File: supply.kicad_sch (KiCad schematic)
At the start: 156 parts, among them J7 BarrelJack_3167288, J8 JST_SH_1x4_BM04B-SRSS-TB-LF-SN, Q12 SI7613DN-T1-GE3, Q13 SI7613DN-T1-GE3, Q14 BSS138PW, Q15 BSS138PW, Q16 BSS138PW, Q17 BSS138PW, SW4 SW_CVS-08TB, SW5 SW_KMR211NGLFS_SMD, U17 LTC4412IS6, U18 LTC4412IS6, U19 MPM54304GMN, U20 MPM54304GMN, U21 NCP718BSN330T1G, U22 MAX16150A_SOT, U25 PAC1954T-E_VQFN, U26 MAX812REUS+T, U27 MP8869S, U28 XC6230H001ER-G, U29 MCP4726A0T-E_MAY, U30 PAC1954T-E_VQFN, U31 LM3880

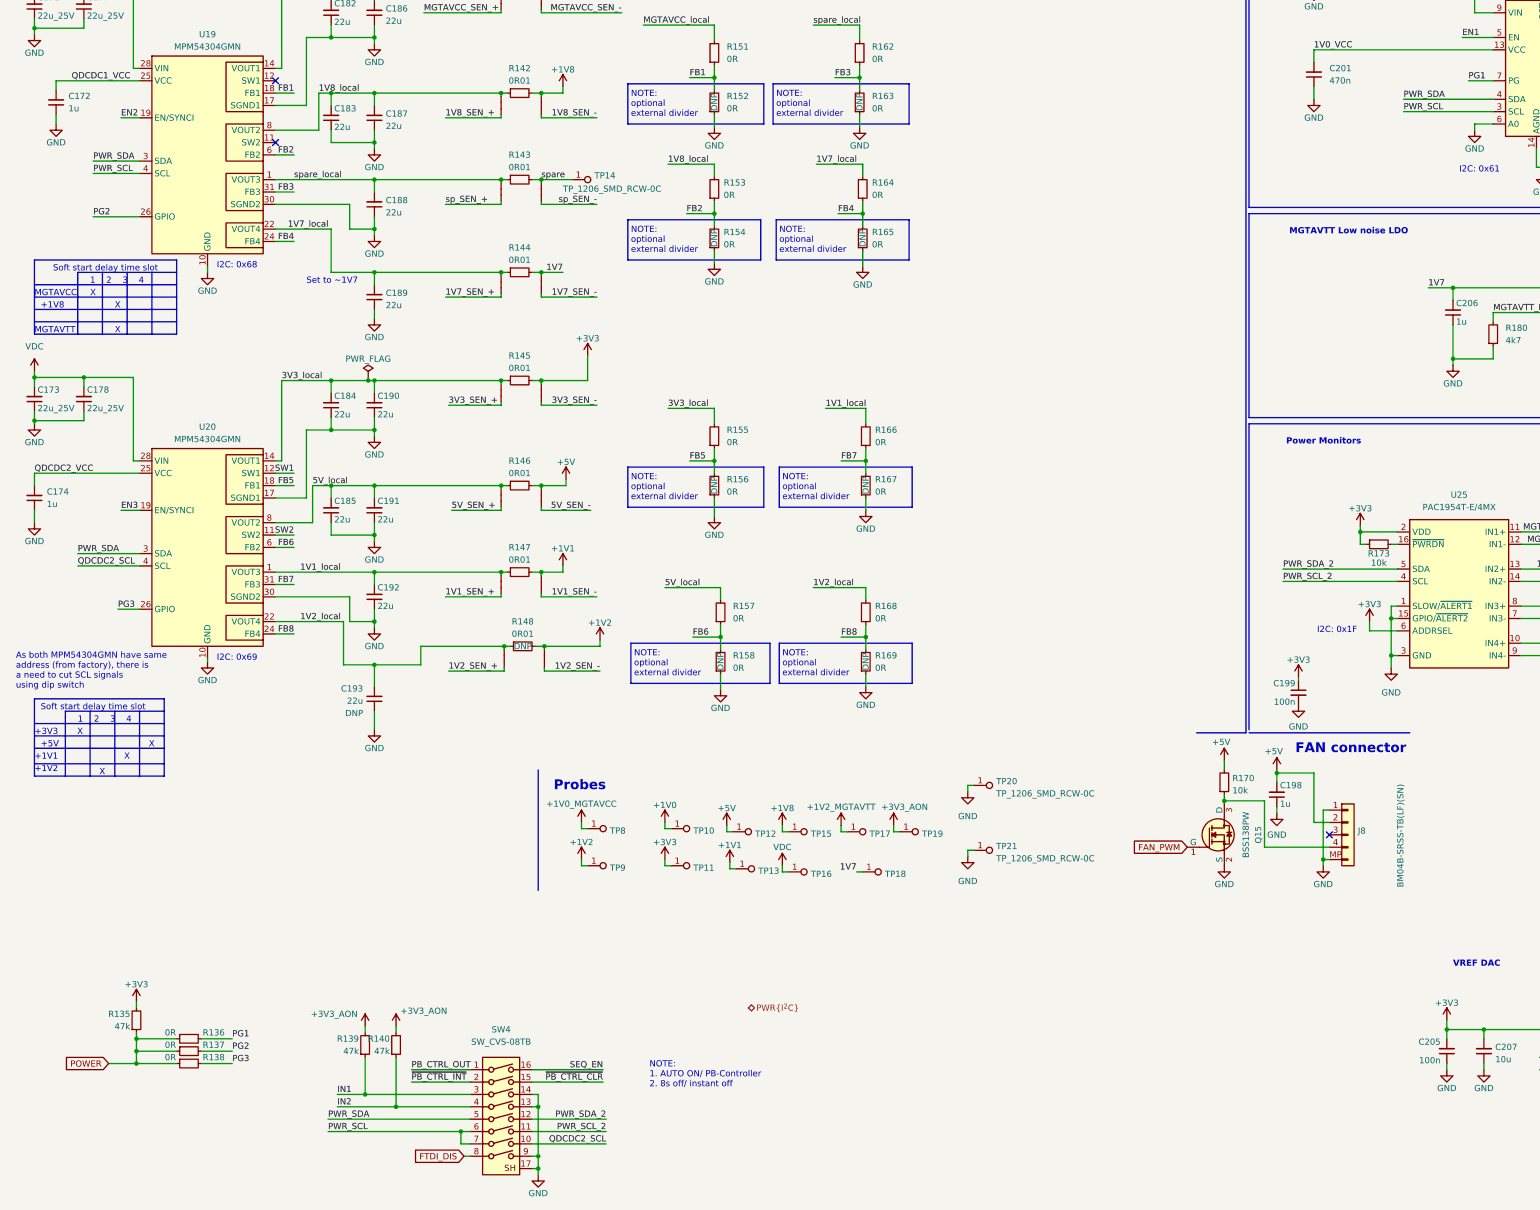
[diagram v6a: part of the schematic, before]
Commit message: Finish reconnecting signals after migration to the hierarchical structure
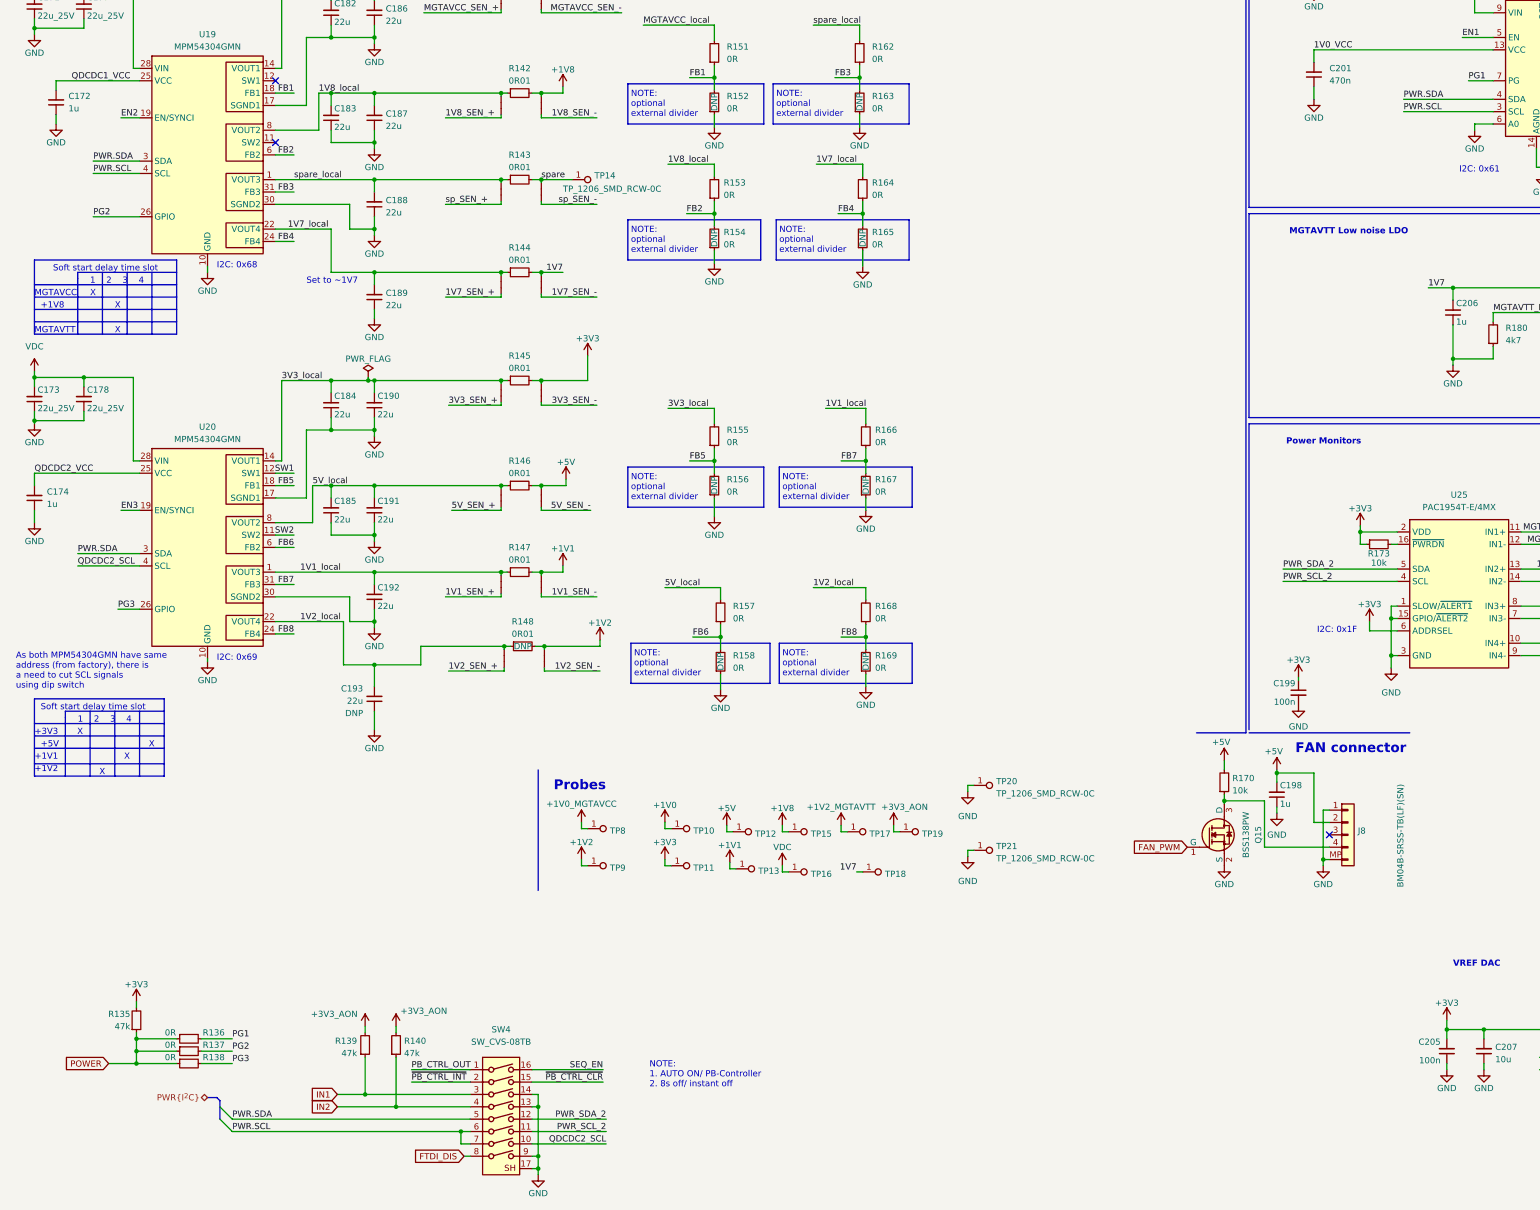
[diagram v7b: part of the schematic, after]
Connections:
- net PWR_SCL renamed PWR.SCL
- net PWR_SDA renamed PWR.SDA
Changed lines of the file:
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@@
   (no_connect (at 85.725 37.465))
   (no_connect (at 66.675 118.745))
+  (bus_entry (at 57.785 332.105) (size -2.54 -2.54)
+    (stroke (width 0) (type default) (color 0 0 0 0))
+  )
+  (bus_entry (at 57.785 334.645) (size -2.54 -2.54)
+    (stroke (width 0) (type default) (color 0 0 0 0))
+  )
   (wire (pts (xy 156.845 194.31) (xy 156.845 196.85))
     (stroke (width 0) (type default) (color 0 0 0 0))
@@
     (stroke (width 0) (type default) (color 0 0 0 0))
   )
+  (bus (pts (xy 52.705 327.66) (xy 54.61 327.66))
+    (stroke (width 0) (type default) (color 0 0 0 0))
+  )
   (wire (pts (xy 121.285 139.065) (xy 127.635 139.065))
     (stroke (width 0) (type default) (color 0 0 0 0))
@@
     (stroke (width 0) (type default) (color 0 0 0 0))
   )
-  (wire (pts (xy 77.47 332.105) (xy 106.68 332.105))
+  (wire (pts (xy 57.785 332.105) (xy 106.68 332.105))
     (stroke (width 0) (type default) (color 0 0 0 0))
   )
@@
     (stroke (width 0) (type default) (color 0 0 0 0))
   )
-  (wire (pts (xy 77.47 334.645) (xy 104.775 334.645))
+  (wire (pts (xy 57.785 334.645) (xy 104.775 334.645))
     (stroke (width 0) (type default) (color 0 0 0 0))
   )
@@
     (stroke (width 0) (type default) (color 0 0 0 0))
   )
+  (bus (pts (xy 54.61 327.66) (xy 55.245 328.295))
+    (stroke (width 0) (type default) (color 0 0 0 0))
+  )
   (wire (pts (xy 182.88 196.85) (xy 187.96 196.85))
     (stroke (width 0) (type default) (color 0 0 0 0))
@@
     (stroke (width 0) (type default) (color 0 0 0 0))
   )
+  (bus (pts (xy 55.245 329.565) (xy 55.245 332.105))
+    (stroke (width 0) (type default) (color 0 0 0 0))
+  )
   (wire (pts (xy 29.21 135.255) (xy 38.735 135.255))
     (stroke (width 0) (type default) (color 0 0 0 0))
@@
     (stroke (width 0) (type default) (color 0 0 0 0))
   )
+  (bus (pts (xy 55.245 328.295) (xy 55.245 329.565))
+    (stroke (width 0) (type default) (color 0 0 0 0))
+  )
   (wire (pts (xy 281.94 268.605) (xy 281.94 278.765))
     (stroke (width 0) (type default) (color 0 0 0 0))
@@
     (effects (font (size 1.27 1.27)) (justify right bottom))
   )
-  (label "IN1" (at 79.375 327.025 0)
-    (effects (font (size 1.27 1.27)) (justify left bottom))
-  )
   (label "~{PB_CTRL_CLR}" (at 133.985 324.485 180)
     (effects (font (size 1.27 1.27)) (justify right bottom))
   )
+  (label "PWR.SDA" (at 57.785 332.105 0)
+    (effects (font (size 1.27 1.27)) (justify left bottom))
+  )
   (label "5V_SEN_-" (at 404.495 221.615 180)
     (effects (font (size 1.27 1.27)) (justify right bottom))
   )
-  (label "PWR_SDA" (at 77.47 332.105 0)
-    (effects (font (size 1.27 1.27)) (justify left bottom))
-  )
   (label "PWR_SDA_2" (at 347.345 219.075 0)
     (effects (font (size 1.27 1.27)) (justify left bottom))
@@
     (effects (font (size 1.27 1.27)) (justify left bottom))
   )
+  (label "PWR.SCL" (at 57.785 334.645 0)
+    (effects (font (size 1.27 1.27)) (justify left bottom))
+  )
   (label "12V_PCIE_fused" (at 60.325 55.245 0)
     (effects (font (size 1.27 1.27)) (justify left bottom))
@@
     (effects (font (size 1.27 1.27)) (justify left bottom))
   )
-  (label "IN2" (at 79.375 329.565 0)
-    (effects (font (size 1.27 1.27)) (justify left bottom))
-  )
   (label "FB5" (at 70.485 201.93 180)
     (effects (font (size 1.27 1.27)) (justify right bottom))
@@
     (effects (font (size 1.27 1.27)) (justify right bottom))
   )
-  (label "PWR_SDA" (at 298.45 122.555 0)
+  (label "PWR.SDA" (at 298.45 122.555 0)
     (effects (font (size 1.27 1.27)) (justify left bottom))
   )
@@
     (effects (font (size 1.27 1.27)) (justify left bottom))
   )
-  (label "PWR_SCL" (at 29.21 137.795 0)
+  (label "PWR.SCL" (at 29.21 137.795 0)
     (effects (font (size 1.27 1.27)) (justify left bottom))
   )
@@
     (effects (font (size 1.27 1.27)) (justify left bottom))
   )
-  (label "PWR_SDA" (at 26.035 215.9 0)
+  (label "PWR.SDA" (at 26.035 215.9 0)
     (effects (font (size 1.27 1.27)) (justify left bottom))
   )
@@
     (effects (font (size 1.27 1.27)) (justify right bottom))
   )
-  (label "PWR_SCL" (at 77.47 334.645 0)
-    (effects (font (size 1.27 1.27)) (justify left bottom))
-  )
-  (label "PWR_SDA" (at 29.21 135.255 0)
+  (label "PWR.SDA" (at 29.21 135.255 0)
     (effects (font (size 1.27 1.27)) (justify left bottom))
   )
@@
     (effects (font (size 1.27 1.27)) (justify right bottom))
   )
-  (label "PWR_SCL" (at 298.45 125.095 0)
+  (label "PWR.SCL" (at 298.45 125.095 0)
     (effects (font (size 1.27 1.27)) (justify left bottom))
   )
@@
     (effects (font (size 1.27 1.27)) (justify right))
     (property "Intersheet References" "${INTERSHEET_REFS}" (id 0) (at 243.0277 276.1456 0)
-      (effects (font (size 1.27 1.27)) (justify right) hide)
+      (effects (font (size 1.27 1.27)) (justify right))
     )
   )
@@
     (effects (font (size 1.27 1.27)) (justify right))
     (property "Intersheet References" "${INTERSHEET_REFS}" (id 0) (at 239.7318 53.2606 0)
-      (effects (font (size 1.27 1.27)) (justify right) hide)
+      (effects (font (size 1.27 1.27)) (justify right))
     )
   )
@@
     (effects (font (size 1.27 1.27)) (justify left))
     (property "Intersheet References" "${INTERSHEET_REFS}" (id 0) (at 397.5966 309.8006 0)
-      (effects (font (size 1.27 1.27)) (justify left) hide)
+      (effects (font (size 1.27 1.27)) (justify left))
     )
   )
@@
     (effects (font (size 1.27 1.27)) (justify right))
     (property "Intersheet References" "${INTERSHEET_REFS}" (id 0) (at 198.8498 67.8656 0)
-      (effects (font (size 1.27 1.27)) (justify right) hide)
+      (effects (font (size 1.27 1.27)) (justify right))
     )
   )
@@
     (effects (font (size 1.27 1.27)) (justify right))
     (property "Intersheet References" "${INTERSHEET_REFS}" (id 0) (at 95.014 339.6456 0)
-      (effects (font (size 1.27 1.27)) (justify right) hide)
+      (effects (font (size 1.27 1.27)) (justify right))
     )
   )
@@
     (effects (font (size 1.27 1.27)) (justify right))
     (property "Intersheet References" "${INTERSHEET_REFS}" (id 0) (at 23.5898 320.5956 0)
-      (effects (font (size 1.27 1.27)) (justify right) hide)
+      (effects (font (size 1.27 1.27)) (justify right))
     )
   )
-  (hierarchical_label "PWR{I^{2}C}" (shape bidirectional) (at 163.83 309.245 0)
-    (effects (font (size 1.27 1.27)) (justify left))
+  (global_label "IN1" (shape input) (at 79.375 327.025 180) (fields_autoplaced)
+    (effects (font (size 1.27 1.27)) (justify right))
+    (property "Intersheet References" "${INTERSHEET_REFS}" (id 0) (at 73.906 327.1044 0)
+      (effects (font (size 1.27 1.27)) (justify right))
+    )
+  )
+  (global_label "IN2" (shape input) (at 79.375 329.565 180) (fields_autoplaced)
+    (effects (font (size 1.27 1.27)) (justify right))
+    (property "Intersheet References" "${INTERSHEET_REFS}" (id 0) (at 73.906 329.4856 0)
+      (effects (font (size 1.27 1.27)) (justify right))
+    )
+  )
+  (hierarchical_label "PWR{I^{2}C}" (shape bidirectional) (at 52.705 327.66 180)
+    (effects (font (size 1.27 1.27)) (justify right))
   )
   (symbol (lib_id "sodimm-ddr5-tester:TP_1mm_SMD") (at 160.655 273.05 0) (unit 1)
@@
   (symbol (lib_id "antmicropower:+12V") (at 34.29 53.975 0) (unit 1)
     (in_bom yes) (on_board yes) (fields_autoplaced)
-    (property "Reference" "#PWR?" (id 0) (at 34.29 57.785 0)
+    (property "Reference" "#PWR0421" (id 0) (at 34.29 57.785 0)
       (effects (font (size 1.27 1.27)) hide)
     )
@@
   )
   (symbol (lib_id "sodimm-ddr5-tester:R_47k_0402") (at 85.09 319.405 90) (unit 1)
-    (in_bom yes) (on_board yes)
-    (property "Reference" "R139" (id 0) (at 83.82 315.595 90)
+    (in_bom yes) (on_board yes) (fields_autoplaced)
+    (property "Reference" "R139" (id 0) (at 83.439 316.0344 90)
       (effects (font (size 1.27 1.27)) (justify left))
     )
@@
       (effects (font (size 1.27 1.27) (thickness 0.15)) (justify left bottom) hide)
     )
-    (property "Val" "47k" (id 6) (at 83.82 318.135 90)
+    (property "Val" "47k" (id 6) (at 83.439 318.5647 90)
       (effects (font (size 1.27 1.27) (thickness 0.15)) (justify left))
     )
@@
   )
   (symbol (lib_id "sodimm-ddr5-tester:R_47k_0402") (at 91.44 319.405 90) (unit 1)
-    (in_bom yes) (on_board yes)
-    (property "Reference" "R140" (id 0) (at 90.17 315.595 90)
-      (effects (font (size 1.27 1.27)) (justify left))
+    (in_bom yes) (on_board yes) (fields_autoplaced)
+    (property "Reference" "R140" (id 0) (at 93.091 316.0344 90)
+      (effects (font (size 1.27 1.27)) (justify right))
     )
     (property "Value" "R_47k_0402" (id 1) (at 104.14 299.085 0)
@@
       (effects (font (size 1.27 1.27) (thickness 0.15)) (justify left bottom) hide)
     )
-    (property "Val" "47k" (id 6) (at 90.17 318.135 90)
-      (effects (font (size 1.27 1.27) (thickness 0.15)) (justify left))
+    (property "Val" "47k" (id 6) (at 93.091 318.5647 90)
+      (effects (font (size 1.27 1.27) (thickness 0.15)) (justify right))
     )
     (property "License" "Apache-2.0" (id 7) (at 116.84 299.085 0)
